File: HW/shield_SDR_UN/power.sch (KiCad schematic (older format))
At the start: 0 parts

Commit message: adicion potencia usb y osc procesador
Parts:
- added C? (x6): 4.7uF, symbol Device:C
- added C?: 22uF, modules:C_0805_HandSoldering, symbol Device:C
- added C?: 0.1uF, Capacitor_SMD:C_0402_1005Metric, symbol Device:C
- added D?: D_Zener--5.1V 1W, symbol Device:D_Zener
- added FB? (x2): FILTER, symbol hackrf-one-packages:FILTER
- added J?: USB_B_Micro, symbol Connector:USB_B_Micro
- added J?: USB_A, symbol Connector:USB_A
- added L?: L, symbol Device:L
- added U? (x3): LT1117CST, symbol Project:LT1117CST
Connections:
- net labels added: +5V, 1V2 FPGA, 3V3 FPGA, 3v3 MCU, GND, USB_D+, USB_D-
- wire segments 0 -> 71
- no-connect marks 0 -> 3

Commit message: MAX2830 Symbol/Footprint created
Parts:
- U? (x3): symbol Project:LT1117CST -> shield_SDR_UN-rescue:LT1117CST-Project
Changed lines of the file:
@@
 $EndDescr
 $Comp
-L Project:LT1117CST U?
+L shield_SDR_UN-rescue:LT1117CST-Project U?
 U 1 1 5CCD0ED3
 P 2350 4900
+AR Path="/5CCD0ED3" Ref="U?"  Part="1"
+AR Path="/5CC08321/5CCD0ED3" Ref="U?"  Part="1"
 F 0 "U?" H 2325 5307 60  0000 C CNN
 F 1 "LT1117CST" H 2325 5216 40  0000 C CNN
@@
 	1500 5250 1500 5100
 $Comp
-L Project:LT1117CST U?
+L shield_SDR_UN-rescue:LT1117CST-Project U?
 U 1 1 5CCEB9EC
 P 2350 6150
+AR Path="/5CCEB9EC" Ref="U?"  Part="1"
+AR Path="/5CC08321/5CCEB9EC" Ref="U?"  Part="1"
 F 0 "U?" H 2325 6557 60  0000 C CNN
 F 1 "LT1117CST" H 2325 6466 40  0000 C CNN
@@
 	1500 6500 1500 6350
 $Comp
-L Project:LT1117CST U?
+L shield_SDR_UN-rescue:LT1117CST-Project U?
 U 1 1 5CD3AA56
 P 2400 3450
+AR Path="/5CD3AA56" Ref="U?"  Part="1"
+AR Path="/5CC08321/5CD3AA56" Ref="U?"  Part="1"
 F 0 "U?" H 2375 3857 60  0000 C CNN
 F 1 "LT1117CST" H 2375 3766 40  0000 C CNN
@@
 $Comp
 L Connector:USB_A J?
-U 0 0 5D029612
+U 1 1 5D029612
 P 5400 3450
 F 0 "J?" H 5457 3917 50  0000 C CNN
@@
 F 3 "" H 5550 3400 50  0001 C CNN
 F 4 "https://www.digikey.com/product-detail/en/amphenol-icc-commercial-products/UE27AC54100/UE27AC54100-ND/1972253" H 5400 3450 50  0001 C CNN "digikey"
-	0    5400 3450
+	1    5400 3450
 	1    0    0    -1
 $EndComp
 $Comp
 L Device:D_Zener D?
-U 0 0 5D02DDAB
+U 1 1 5D02DDAB
 P 6100 2800
 F 0 "D?" V 6054 2879 50  0000 L CNN
@@
 F 2 "" H 6100 2800 50  0001 C CNN
 F 3 "~" H 6100 2800 50  0001 C CNN
-	0    6100 2800
+	1    6100 2800
 	0    1    1    0
 $EndComp
 $Comp
 L Device:C C?
-U 0 0 5D02F582
+U 1 1 5D02F582
 P 6650 2800
 F 0 "C?" H 6765 2846 50  0000 L CNN
@@
 F 2 "modules:C_0805_HandSoldering" H 6688 2650 50  0001 C CNN
 F 3 "~" H 6650 2800 50  0001 C CNN
-	0    6650 2800
-	1    0    0    -1
-$EndComp
-$Comp
-L Device:C C?
-U 0 0 5D02FD2B
+	1    6650 2800
+	1    0    0    -1
+$EndComp
+$Comp
+L Device:C C?
+U 1 1 5D02FD2B
 P 7100 2800
 F 0 "C?" H 7215 2846 50  0000 L CNN
@@
 F 2 "Capacitor_SMD:C_0402_1005Metric" H 7138 2650 50  0001 C CNN
 F 3 "~" H 7100 2800 50  0001 C CNN
-	0    7100 2800
+	1    7100 2800
 	1    0    0    -1
 $EndComp
 $Comp
 L Device:L L?
-U 0 0 5D031306
+U 1 1 5D031306
 P 7600 2450
 F 0 "L?" V 7790 2450 50  0000 C CNN
@@
 F 3 "~" H 7600 2450 50  0001 C CNN
 F 4 "732-1593-1-ND" V 7600 2450 50  0001 C CNN "digikey"
-	0    7600 2450
+	1    7600 2450
 	0    -1   -1   0
 $EndComp
@@
 $Comp
 L hackrf-one-packages:FILTER FB?
-U 0 0 5D03DEDD
+U 1 1 5D03DEDD
 P 7050 3550
 F 0 "FB?" H 7050 3790 50  0000 C CNN
@@
 F 3 "" H 7050 3550 60  0000 C CNN
 F 4 "SRF2012-900YACT-ND " H 7050 3550 50  0001 C CNN "DIGIKEY"
-	0    7050 3550
+	1    7050 3550
 	1    0    0    -1
 $EndComp
 $Comp
 L hackrf-one-packages:FILTER FB?
-U 0 0 5D03FEE7
+U 1 1 5D03FEE7
 P 7050 3900
 F 0 "FB?" H 7050 4140 50  0000 C CNN
@@
 F 3 "" H 7050 3900 60  0000 C CNN
 F 4 "SRF2012-900YACT-ND " H 7050 3900 50  0001 C CNN "DIGIKEY"
-	0    7050 3900
-	1    0    0    -1
-$EndComp
+	1    7050 3900
+	1    0    0    -1
+$EndComp

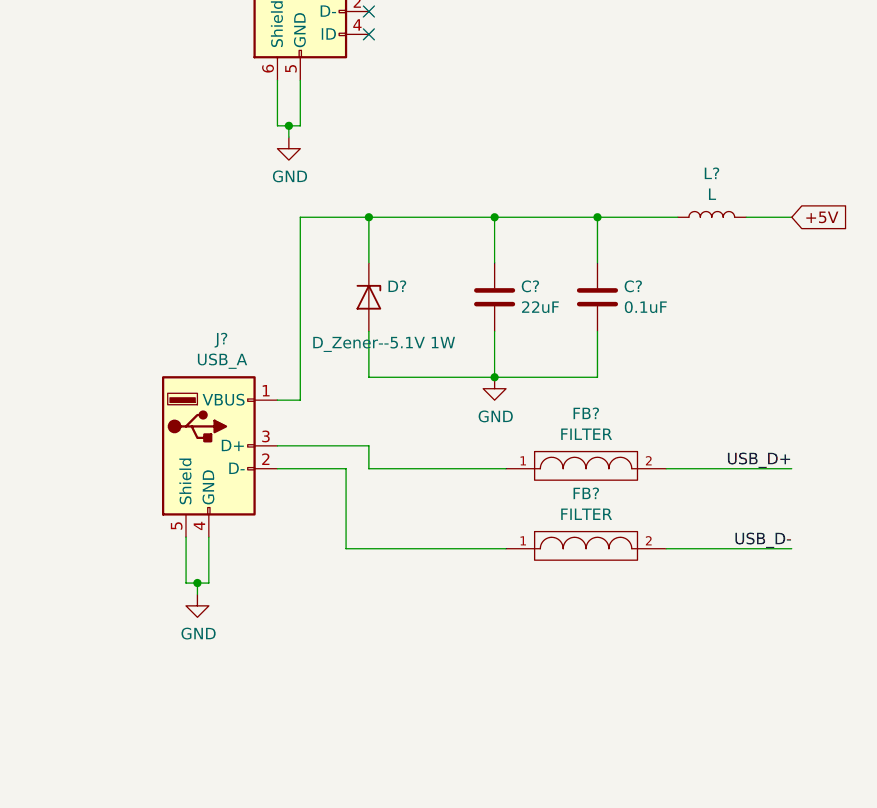
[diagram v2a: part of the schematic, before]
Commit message: Onion 2 routed
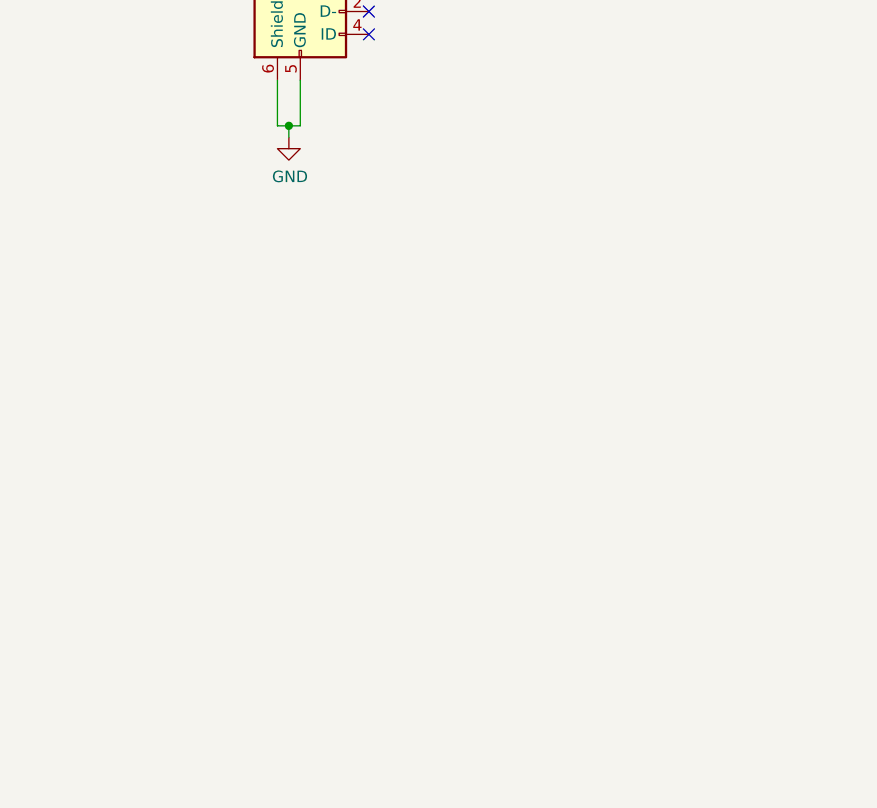
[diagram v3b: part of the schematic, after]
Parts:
- removed C?: 22uF, modules:C_0805_HandSoldering, symbol Device:C
- removed C?: 0.1uF, Capacitor_SMD:C_0402_1005Metric, symbol Device:C
- removed D?: D_Zener--5.1V 1W, symbol Device:D_Zener
- removed FB? (x2): FILTER, symbol hackrf-one-packages:FILTER
- removed J?: USB_A, symbol Connector:USB_A
- removed L?: L, symbol Device:L
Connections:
- net labels removed: USB_D+, USB_D-
- wire segments 71 -> 43
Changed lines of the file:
@@
 $Descr A4 11693 8268
 encoding utf-8
-Sheet 5 5
+Sheet 5 6
 Title ""
 Date ""
@@
 Wire Wire Line
 	1550 3800 1550 3650
-Text GLabel 3200 2900 1    50   Output ~ 0
-3v3 MCU
 Wire Wire Line
 	3200 2900 3200 3250
@@
 Wire Wire Line
 	1300 5800 1300 5950
-$Comp
-L Connector:USB_A J?
-U 1 1 5D029612
-P 5400 3450
-F 0 "J?" H 5457 3917 50  0000 C CNN
-F 1 "USB_A" H 5457 3826 50  0000 C CNN
-F 2 "" H 5550 3400 50  0001 C CNN
-F 3 "" H 5550 3400 50  0001 C CNN
-F 4 "https://www.digikey.com/product-detail/en/amphenol-icc-commercial-products/UE27AC54100/UE27AC54100-ND/1972253" H 5400 3450 50  0001 C CNN "digikey"
-	1    5400 3450
-	1    0    0    -1
-$EndComp
-$Comp
-L Device:D_Zener D?
-U 1 1 5D02DDAB
-P 6100 2800
-F 0 "D?" V 6054 2879 50  0000 L CNN
-F 1 "D_Zener--5.1V 1W" V 6300 2550 50  0000 L CNN
-F 2 "" H 6100 2800 50  0001 C CNN
-F 3 "~" H 6100 2800 50  0001 C CNN
-	1    6100 2800
-	0    1    1    0
-$EndComp
-$Comp
-L Device:C C?
-U 1 1 5D02F582
-P 6650 2800
-F 0 "C?" H 6765 2846 50  0000 L CNN
-F 1 "22uF" H 6765 2755 50  0000 L CNN
-F 2 "modules:C_0805_HandSoldering" H 6688 2650 50  0001 C CNN
-F 3 "~" H 6650 2800 50  0001 C CNN
-	1    6650 2800
-	1    0    0    -1
-$EndComp
-$Comp
-L Device:C C?
-U 1 1 5D02FD2B
-P 7100 2800
-F 0 "C?" H 7215 2846 50  0000 L CNN
-F 1 "0.1uF" H 7215 2755 50  0000 L CNN
-F 2 "Capacitor_SMD:C_0402_1005Metric" H 7138 2650 50  0001 C CNN
-F 3 "~" H 7100 2800 50  0001 C CNN
-	1    7100 2800
-	1    0    0    -1
-$EndComp
-$Comp
-L Device:L L?
-U 1 1 5D031306
-P 7600 2450
-F 0 "L?" V 7790 2450 50  0000 C CNN
-F 1 "L" V 7699 2450 50  0000 C CNN
-F 2 "" H 7600 2450 50  0001 C CNN
-F 3 "~" H 7600 2450 50  0001 C CNN
-F 4 "732-1593-1-ND" V 7600 2450 50  0001 C CNN "digikey"
-	1    7600 2450
-	0    -1   -1   0
-$EndComp
-Wire Wire Line
-	7450 2450 7100 2450
-Wire Wire Line
-	6100 2450 6100 2650
-Wire Wire Line
-	6650 2650 6650 2450
-Connection ~ 6650 2450
-Wire Wire Line
-	6650 2450 6100 2450
-Wire Wire Line
-	7100 2650 7100 2450
-Connection ~ 7100 2450
-Wire Wire Line
-	7100 2450 6650 2450
-$Comp
-L power:GND #PWR?
-U 1 1 5D033245
-P 6650 3150
-F 0 "#PWR?" H 6650 2900 50  0001 C CNN
-F 1 "GND" H 6655 2977 50  0000 C CNN
-F 2 "" H 6650 3150 50  0001 C CNN
-F 3 "" H 6650 3150 50  0001 C CNN
-	1    6650 3150
-	1    0    0    -1
-$EndComp
-Wire Wire Line
-	6650 3150 6100 3150
-Wire Wire Line
-	6100 2950 6100 3150
-Wire Wire Line
-	6650 3150 6650 2950
-Connection ~ 6650 3150
-Wire Wire Line
-	6650 3150 7100 3150
-Wire Wire Line
-	7100 3150 7100 2950
-Text GLabel 7950 2450 2    50   Input ~ 0
-+5V
-Wire Wire Line
-	7950 2450 7750 2450
-Wire Wire Line
-	5700 3250 5800 3250
-Wire Wire Line
-	5800 3250 5800 2450
-Wire Wire Line
-	5800 2450 6100 2450
-Connection ~ 6100 2450
-Wire Wire Line
-	5300 3850 5300 4050
-Wire Wire Line
-	5300 4050 5350 4050
-Wire Wire Line
-	5400 4050 5400 3850
-$Comp
-L power:GND #PWR?
-U 1 1 5D03CDB0
-P 5350 4100
-F 0 "#PWR?" H 5350 3850 50  0001 C CNN
-F 1 "GND" H 5355 3927 50  0000 C CNN
-F 2 "" H 5350 4100 50  0001 C CNN
-F 3 "" H 5350 4100 50  0001 C CNN
-	1    5350 4100
-	1    0    0    -1
-$EndComp
-Wire Wire Line
-	5350 4100 5350 4050
-Connection ~ 5350 4050
-Wire Wire Line
-	5350 4050 5400 4050
-$Comp
-L hackrf-one-packages:FILTER FB?
-U 1 1 5D03DEDD
-P 7050 3550
-F 0 "FB?" H 7050 3790 50  0000 C CNN
-F 1 "FILTER" H 7050 3699 50  0000 C CNN
-F 2 "" H 7050 3550 60  0000 C CNN
-F 3 "" H 7050 3550 60  0000 C CNN
-F 4 "SRF2012-900YACT-ND " H 7050 3550 50  0001 C CNN "DIGIKEY"
-	1    7050 3550
-	1    0    0    -1
-$EndComp
-$Comp
-L hackrf-one-packages:FILTER FB?
-U 1 1 5D03FEE7
-P 7050 3900
-F 0 "FB?" H 7050 4140 50  0000 C CNN
-F 1 "FILTER" H 7050 4049 50  0000 C CNN
-F 2 "" H 7050 3900 60  0000 C CNN
-F 3 "" H 7050 3900 60  0000 C CNN
-F 4 "SRF2012-900YACT-ND " H 7050 3900 50  0001 C CNN "DIGIKEY"
-	1    7050 3900
-	1    0    0    -1
-$EndComp
-Wire Wire Line
-	6700 3550 6100 3550
-Wire Wire Line
-	6100 3550 6100 3450
-Wire Wire Line
-	6100 3450 5700 3450
-Wire Wire Line
-	6700 3900 6000 3900
-Wire Wire Line
-	6000 3900 6000 3550
-Wire Wire Line
-	6000 3550 5700 3550
-Wire Wire Line
-	7400 3550 7950 3550
-Wire Wire Line
-	7400 3900 7950 3900
-Text Label 7950 3550 2    50   ~ 0
-USB_D+
-Text Label 7950 3900 2    50   ~ 0
-USB_D-
+Text GLabel 3200 2900 1    50   Output ~ 0
+3v3 MCU
 $EndSCHEMATC

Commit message: Voltage regulators updated
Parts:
- removed U? (x3): LT1117CST, symbol shield_SDR_UN-rescue:LT1117CST-Project
- added D? (x3): LED, symbol Device:LED
- added R? (x3): 1.8k, symbol Device:R
- added U? (x2): ZLDO1117G33TA, Package_TO_SOT_SMD:SOT-223, symbol ZLDO1117:ZLDO1117G33TA
- added U?: ZLDO1117G12TA, Package_TO_SOT_SMD:SOT-223, symbol ZLDO1117:ZLDO1117G12TA
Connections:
- wire segments 43 -> 39
- no-connect marks 3 -> 6
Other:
- note added: "Debug LEDs"
- note added: "FPGA 1.2V Regulator"
- note added: "FPGA 3.3V Regulator"
- note added: "Green\n"
- note added: "Input USB power"
- note added: "MCU 3.3V Regulator"
- note added: "Red"
- moved on the sheet: C?, J?

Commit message: Footprint of voltaje regulators edited
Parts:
- U? (x3): footprint Package_TO_SOT_SMD:SOT-223 -> Package_TO_SOT_SMD:SOT-223-3_TabPin2
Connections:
- net GND: now also U?.1 (GND), U?.1 (GND), U?.1 (GND)
- no-connect marks 6 -> 3
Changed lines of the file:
@@
-$EndComp
-$Comp
-L ZLDO1117:ZLDO1117G33TA U?
-U 1 1 5CDBD7C5
-P 2500 1900
-F 0 "U?" H 2500 2387 60  0000 C CNN
-F 1 "ZLDO1117G33TA" H 2500 2281 60  0000 C CNN
-F 2 "Package_TO_SOT_SMD:SOT-223" H 2500 2387 60  0001 C CNN
-F 3 "https://www.diodes.com/assets/Datasheets/ZLDO1117.pdf" H 2500 2281 60  0001 C CNN
-F 4 "ZLDO1117G33DICT-ND" H 2500 1900 50  0001 C CNN "Digikey"
-	1    2500 1900
-	1    0    0    -1
-$EndComp
-$Comp
-L ZLDO1117:ZLDO1117G12TA U?
-U 1 1 5CDC0021
-P 2500 5050
-F 0 "U?" H 2500 5537 60  0000 C CNN
-F 1 "ZLDO1117G12TA" H 2500 5431 60  0000 C CNN
-F 2 "Package_TO_SOT_SMD:SOT-223" H 2650 5100 60  0001 C CNN
-F 3 "https://www.diodes.com/assets/Datasheets/ZLDO1117.pdf" H 2650 5100 60  0001 C CNN
-F 4 "ZLDO1117G12DICT-ND" H 2500 5050 50  0001 C CNN "Digikey"
-	1    2500 5050
-	1    0    0    -1
-$EndComp
-$Comp
-L power:GND #PWR?
-U 1 1 5CDC2FE1
-P 2350 5550
-F 0 "#PWR?" H 2350 5300 50  0001 C CNN
-F 1 "GND" H 2355 5377 50  0000 C CNN
-F 2 "" H 2350 5550 50  0001 C CNN
-F 3 "" H 2350 5550 50  0001 C CNN
-	1    2350 5550
-	1    0    0    -1
 $EndComp
 $Comp
 L power:GND #PWR?
 U 1 1 5CDC3540
-P 2350 3950
-F 0 "#PWR?" H 2350 3700 50  0001 C CNN
-F 1 "GND" H 2355 3777 50  0000 C CNN
-F 2 "" H 2350 3950 50  0001 C CNN
-F 3 "" H 2350 3950 50  0001 C CNN
-	1    2350 3950
+P 2500 3950
+F 0 "#PWR?" H 2500 3700 50  0001 C CNN
+F 1 "GND" H 2505 3777 50  0000 C CNN
+F 2 "" H 2500 3950 50  0001 C CNN
+F 3 "" H 2500 3950 50  0001 C CNN
+	1    2500 3950
 	1    0    0    -1
 $EndComp
@@
 L power:GND #PWR?
 U 1 1 5CDC3B98
-P 2350 2400
-F 0 "#PWR?" H 2350 2150 50  0001 C CNN
-F 1 "GND" H 2355 2227 50  0000 C CNN
-F 2 "" H 2350 2400 50  0001 C CNN
-F 3 "" H 2350 2400 50  0001 C CNN
-	1    2350 2400
-	1    0    0    -1
-$EndComp
-NoConn ~ 2650 2400
-NoConn ~ 2650 3950
-NoConn ~ 2650 5550
+P 2500 2400
+F 0 "#PWR?" H 2500 2150 50  0001 C CNN
+F 1 "GND" H 2505 2227 50  0000 C CNN
+F 2 "" H 2500 2400 50  0001 C CNN
+F 3 "" H 2500 2400 50  0001 C CNN
+	1    2500 2400
+	1    0    0    -1
+$EndComp
 Wire Wire Line
 	1400 4900 1550 4900
-$Comp
-L ZLDO1117:ZLDO1117G33TA U?
-U 1 1 5CDD0DC2
-P 2500 3450
-F 0 "U?" H 2500 3937 60  0000 C CNN
-F 1 "ZLDO1117G33TA" H 2500 3831 60  0000 C CNN
-F 2 "Package_TO_SOT_SMD:SOT-223" H 2500 3937 60  0001 C CNN
-F 3 "https://www.diodes.com/assets/Datasheets/ZLDO1117.pdf" H 2500 3831 60  0001 C CNN
-F 4 "ZLDO1117G33DICT-ND" H 2500 3450 50  0001 C CNN "Digikey"
-	1    2500 3450
-	1    0    0    -1
-$EndComp
 Wire Wire Line
 	3200 4900 3450 4900
@@
 Text GLabel 6200 3700 1    50   Input ~ 0
 3V3 FPGA
+$Comp
+L ZLDO1117:ZLDO1117G12TA U?
+U 1 1 5CDC0021
+P 2500 5050
+AR Path="/5CDC0021" Ref="U?"  Part="1"
+AR Path="/5CC08321/5CDC0021" Ref="U?"  Part="1"
+F 0 "U?" H 2500 5537 60  0000 C CNN
+F 1 "ZLDO1117G12TA" H 2500 5431 60  0000 C CNN
+F 2 "Package_TO_SOT_SMD:SOT-223-3_TabPin2" H 2650 5100 60  0001 C CNN
+F 3 "https://www.diodes.com/assets/Datasheets/ZLDO1117.pdf" H 2650 5100 60  0001 C CNN
+F 4 "ZLDO1117G12DICT-ND" H 2500 5050 50  0001 C CNN "Digikey"
+	1    2500 5050
+	1    0    0    -1
+$EndComp
+$Comp
+L ZLDO1117:ZLDO1117G33TA U?
+U 1 1 5CDD0DC2
+P 2500 3450
+AR Path="/5CDD0DC2" Ref="U?"  Part="1"
+AR Path="/5CC08321/5CDD0DC2" Ref="U?"  Part="1"
+F 0 "U?" H 2500 3937 60  0000 C CNN
+F 1 "ZLDO1117G33TA" H 2500 3831 60  0000 C CNN
+F 2 "Package_TO_SOT_SMD:SOT-223-3_TabPin2" H 2500 3937 60  0001 C CNN
+F 3 "https://www.diodes.com/assets/Datasheets/ZLDO1117.pdf" H 2500 3831 60  0001 C CNN
+F 4 "ZLDO1117G33DICT-ND" H 2500 3450 50  0001 C CNN "Digikey"
+	1    2500 3450
+	1    0    0    -1
+$EndComp
+$Comp
+L ZLDO1117:ZLDO1117G33TA U?
+U 1 1 5CDBD7C5
+P 2500 1900
+AR Path="/5CDBD7C5" Ref="U?"  Part="1"
+AR Path="/5CC08321/5CDBD7C5" Ref="U?"  Part="1"
+F 0 "U?" H 2500 2387 60  0000 C CNN
+F 1 "ZLDO1117G33TA" H 2500 2281 60  0000 C CNN
+F 2 "Package_TO_SOT_SMD:SOT-223-3_TabPin2" H 2500 2387 60  0001 C CNN
+F 3 "https://www.diodes.com/assets/Datasheets/ZLDO1117.pdf" H 2500 2281 60  0001 C CNN
+F 4 "ZLDO1117G33DICT-ND" H 2500 1900 50  0001 C CNN "Digikey"
+	1    2500 1900
+	1    0    0    -1
+$EndComp
+$Comp
+L power:GND #PWR?
+U 1 1 5CDC2FE1
+P 2500 5550
+F 0 "#PWR?" H 2500 5300 50  0001 C CNN
+F 1 "GND" H 2505 5377 50  0000 C CNN
+F 2 "" H 2500 5550 50  0001 C CNN
+F 3 "" H 2500 5550 50  0001 C CNN
+	1    2500 5550
+	1    0    0    -1
+$EndComp
 $EndSCHEMATC
